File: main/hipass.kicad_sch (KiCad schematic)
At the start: 54 parts, among them U44 TL071, U45 TL071, U46 TL071, U47 TL071, U48 TL071, U49 TL071, U50 TL071, U51 TL071

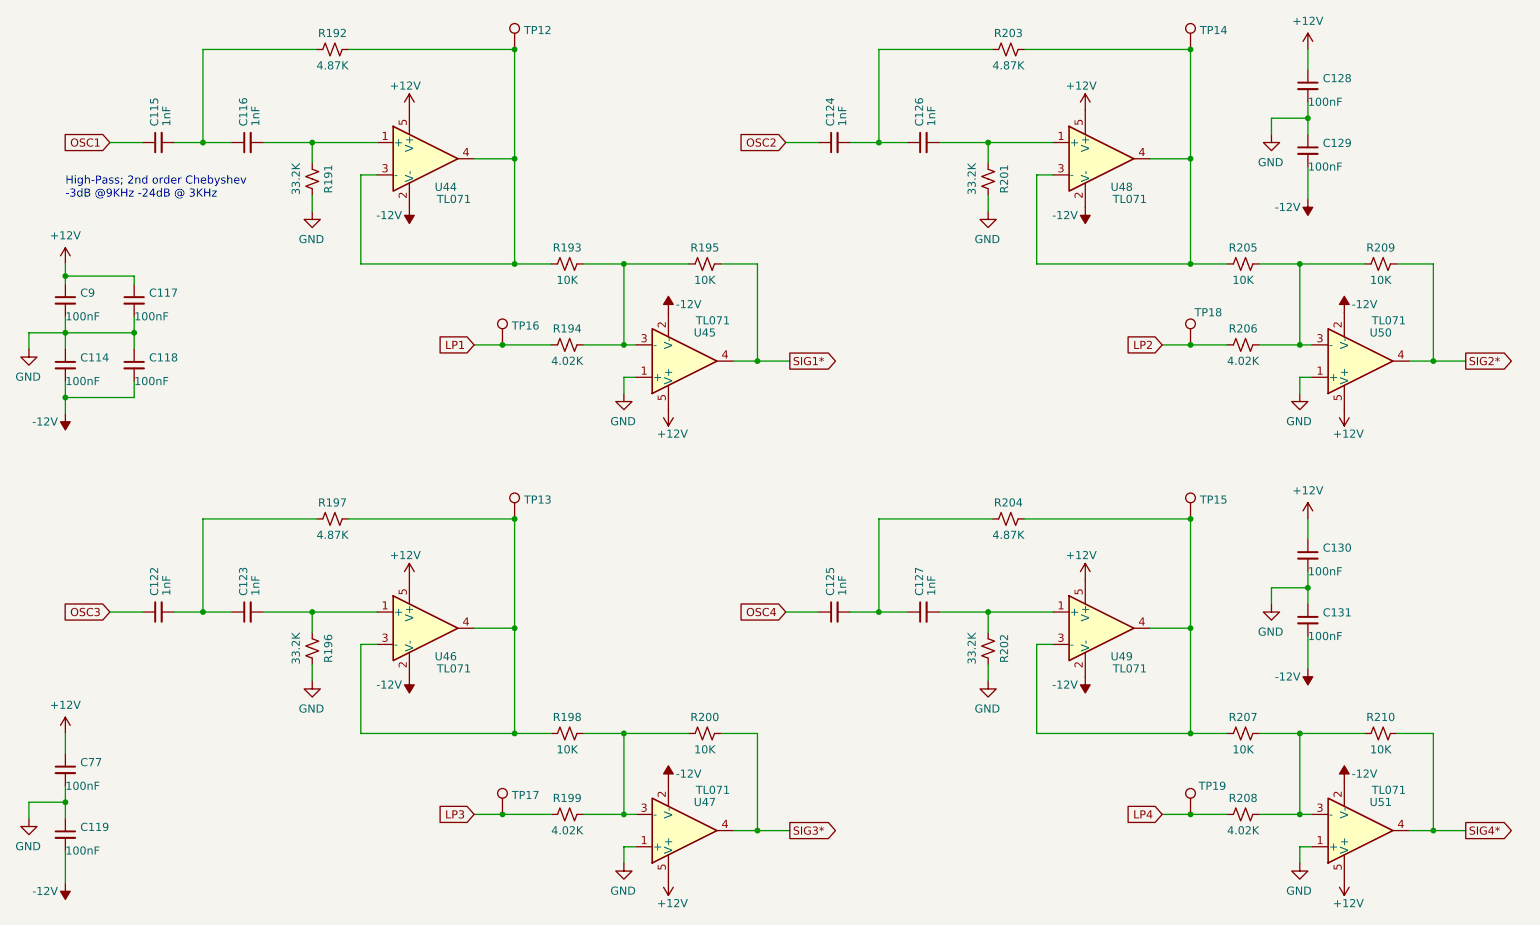
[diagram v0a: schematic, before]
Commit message: v1.0
Docs still need work.
Oscillators.sch not used. Saved just in case.
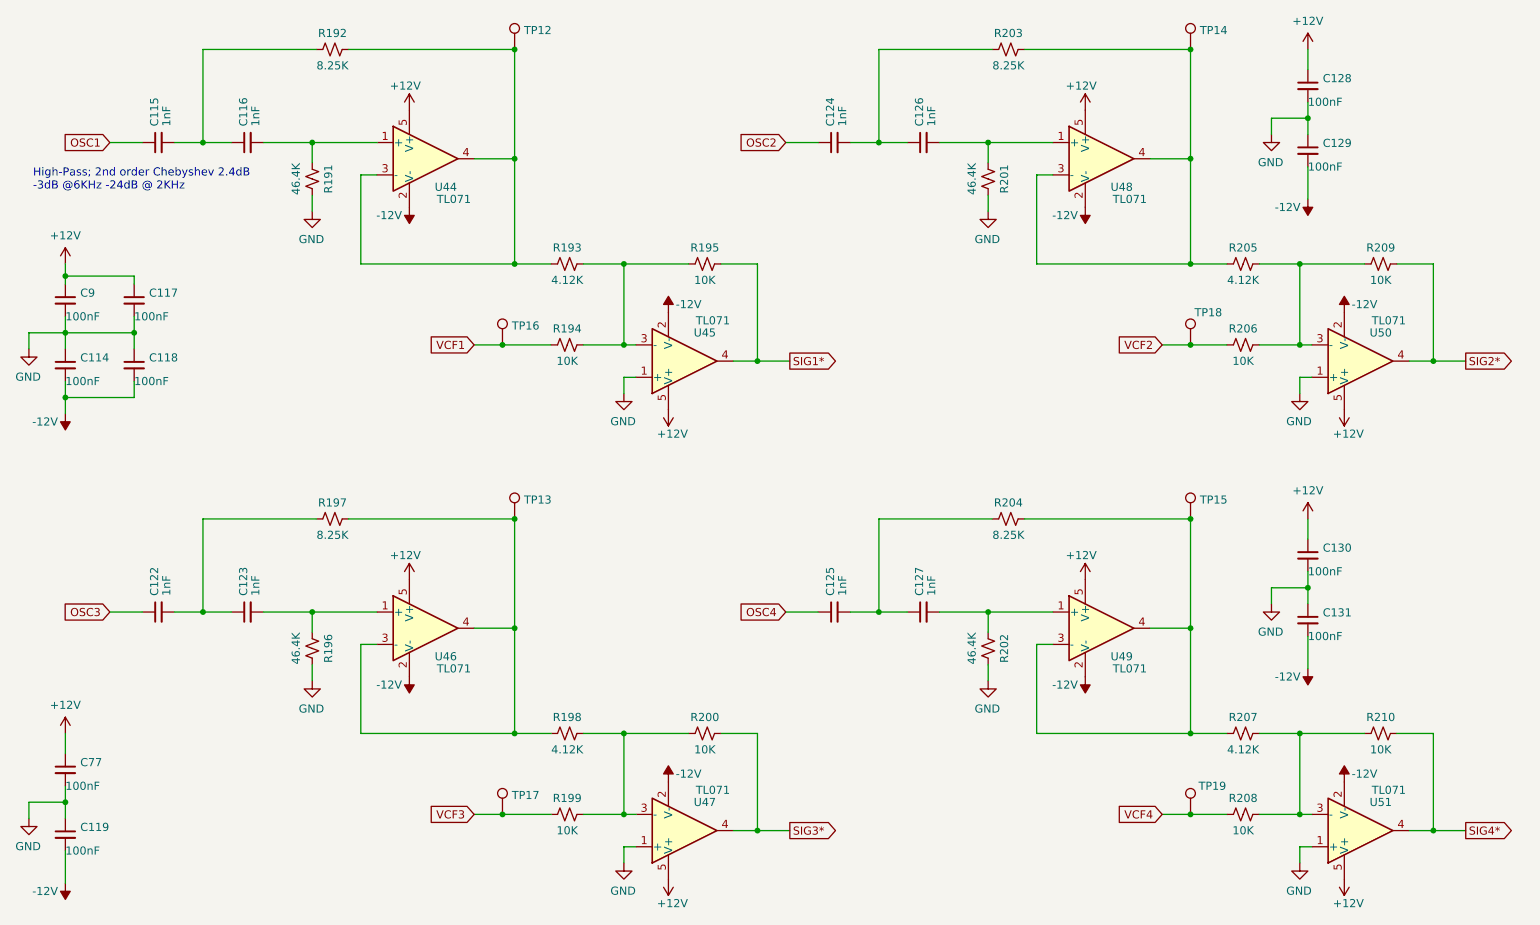
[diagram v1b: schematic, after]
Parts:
- R191, R196, R201, R202: value 33.2K -> 46.4K; LCSC Part # C185338 -> C23059
- R192, R197, R203, R204: value 4.87K -> 8.25K; LCSC Part # C23045 -> C185307
- R193, R198, R205, R207: value 10K -> 4.12K; LCSC Part # C25804 -> C165750
- R194, R199, R206, R208: value 4.02K -> 10K; LCSC Part # C23040 -> C25804
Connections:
- net LP1 renamed VCF1
- net LP2 renamed VCF2
- net LP3 renamed VCF3
- net LP4 renamed VCF4
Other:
- note added: "High-Pass; 2nd order Chebyshev 2.4dB -3dB @6KHz -24dB @ 2KHz"
- note removed: "High-Pass; 2nd order Chebyshev -3dB @9KHz -24dB @ 3KHz"

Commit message: Work in progress
Adds User Manual
Changes CV range to 0 - 8V
Adds spice vactrol test circuit.
Adds VCA spice study
Updates other spice and excel files.
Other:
- title: (none) -> Twangilizer
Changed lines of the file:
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@@
 (kicad_sch (version 20211123) (generator eeschema)
   (paper "A4")
+  (title_block
+    (title "Twangilizer")
+    (rev "1.1")
+  )
   (junction (at 231.14 57.15) (diameter 0) (color 0 0 0 0)
   )
